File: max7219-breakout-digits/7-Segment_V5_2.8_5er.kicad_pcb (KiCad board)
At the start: 2 copper layers, 60 x 12 mm, 6 parts, among them J1 Conn_02x08_Odd_Even, U1 7Segment 3 digit CC_STH, U2 HDSM-443B_CC_2Digit_7Segment_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

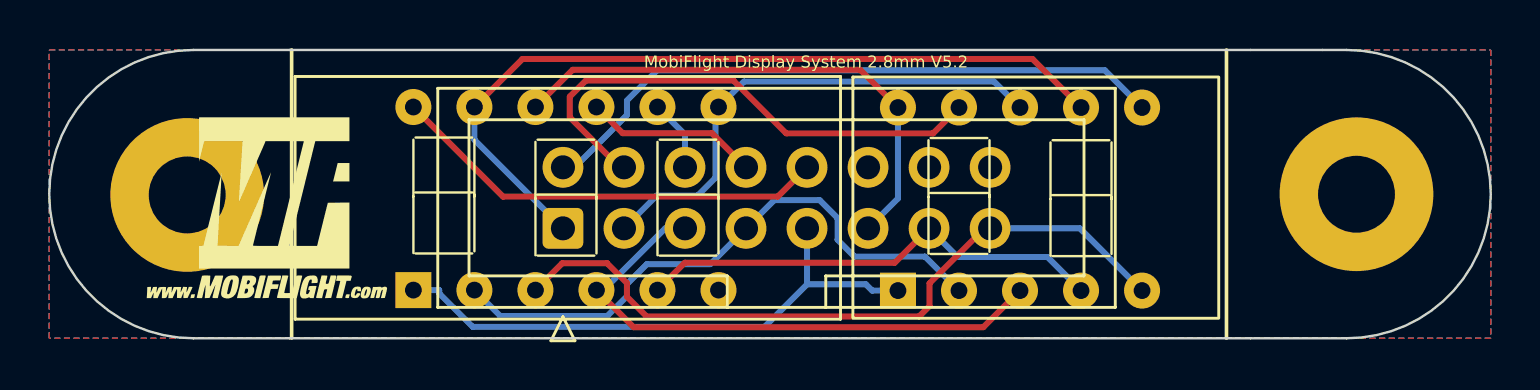
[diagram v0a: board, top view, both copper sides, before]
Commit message: center all mounting holes
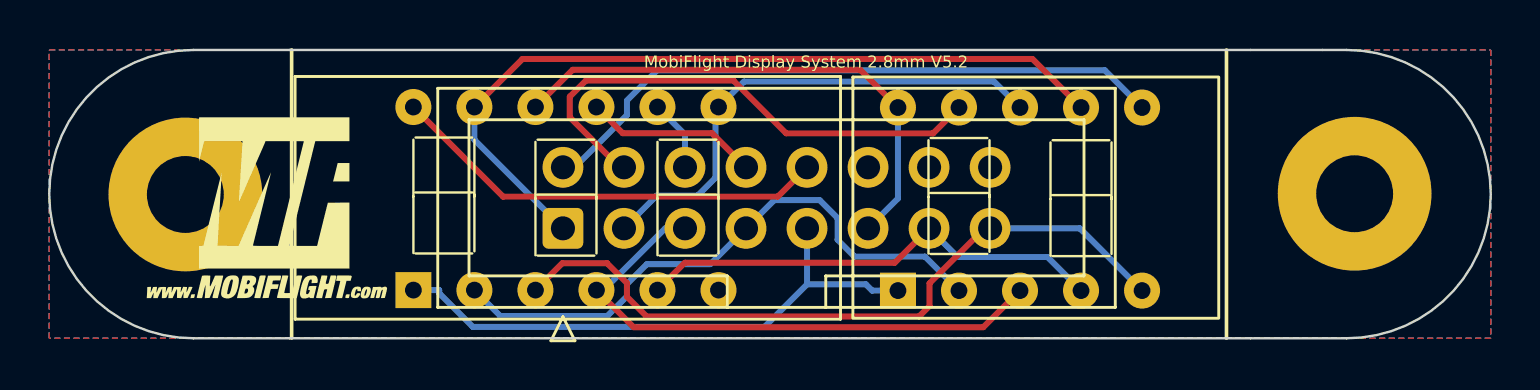
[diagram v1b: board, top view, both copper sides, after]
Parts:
- moved H1 0.08 mm to (71.8, 67.0)
- moved H2 0.08 mm to (120.4, 67.0)
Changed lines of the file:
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@@
 	(footprint "MountingHole:MountingHole_3.2mm_M3_Pad"
 		(layer "F.Cu")
-		(at 120.52 67.03)
+		(at 120.4434 67.0104)
 		(descr "Mounting Hole 3.2mm, M3, generated by kicad-footprint-generator mountinghole.py")
 		(tags "mountinghole M3")
@@
 	(footprint "MountingHole:MountingHole_3.2mm_M3_Pad"
 		(layer "F.Cu")
-		(at 71.85 67.06)
+		(at 71.7734 67.0404)
 		(descr "Mounting Hole 3.2mm, M3, generated by kicad-footprint-generator mountinghole.py")
 		(tags "mountinghole M3")
@@
 		(min_thickness 0.254)
 		(filled_areas_thickness no)
-		(fill
+		(fill yes
 			(thermal_gap 0.508)
 			(thermal_bridge_width 0.508)
@@
 		)
 	)
+	(group ""
+		(members "7358d4fd-9024-47a7-9c53-15a8ffe03d2a" "d40def2e-617a-4ba2-a011-fcf9c19e2675")
+	)
+	(group ""
+		(locked yes)
+		(members "08288747-d5b2-435c-922b-fcc7a7f0bd7c" "250753f3-022a-4620-873d-d2124e2f1f52"
+			"36c7c79c-8914-4db8-a330-b63ab7a2c5dd" "4f09cb32-5a0c-4f44-89e2-81335d9dbf63"
+			"72729664-16c1-4c9c-952c-0f75917eb76d" "816f5a39-a071-4c63-ba02-26157414ef72"
+			"8e475abc-8a56-498c-9e86-1b91522e6052" "9d863c16-ee29-4c67-a2cd-4c5201f270f9"
+			"ecd7cc35-c62f-4821-b112-dd5f689c7683"
+		)
+	)
